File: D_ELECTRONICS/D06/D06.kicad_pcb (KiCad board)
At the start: 2 copper layers, 17.8 x 17.8 mm, 11 parts, among them J4 Conn_01x02_Female, J5 Conn_01x02_Female, Q1 BSS138

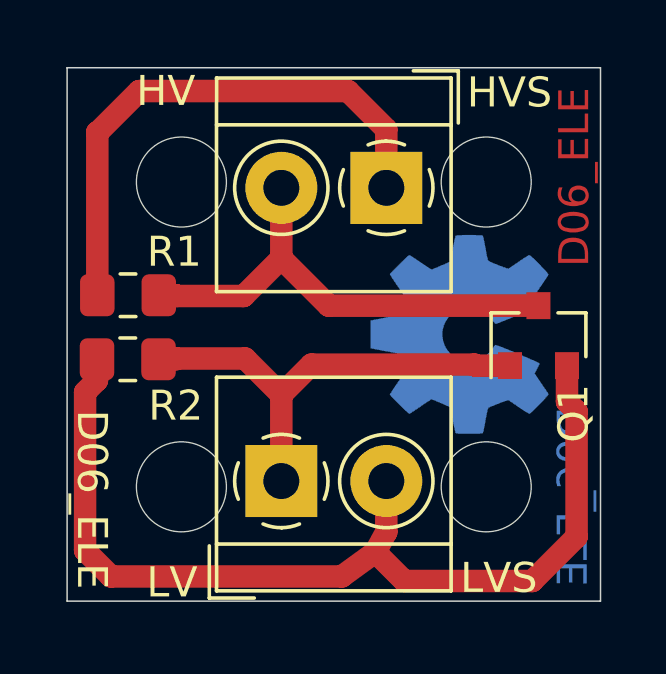
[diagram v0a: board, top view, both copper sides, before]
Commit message: fixed signal trace
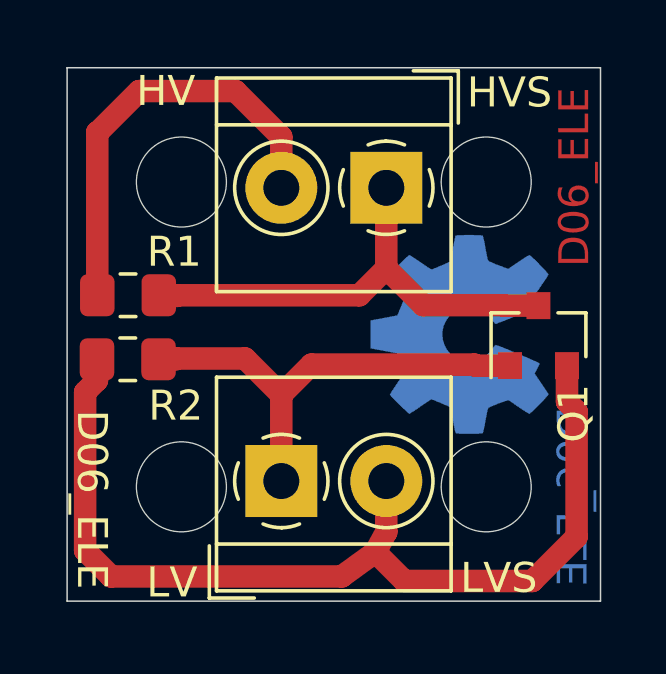
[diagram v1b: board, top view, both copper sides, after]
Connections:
- Q1 pad 3: Net-(J5-Pad2) -> Net-(J5-Pad1)
- R1 pad 1: Net-(J5-Pad1) -> Net-(J5-Pad2)
- R1 pad 2: Net-(J5-Pad2) -> Net-(J5-Pad1)
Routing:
- net Net-(J5-Pad2): track 16.2 -> 14.5 mm
- net Net-(J5-Pad1): track 18.1 -> 16.8 mm
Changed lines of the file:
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@@
     (thickness 1.6)
     (drawings 12)
-    (tracks 36)
+    (tracks 38)
     (zones 0)
     (modules 11)
@@
     (fp_line (start -1 0.6) (end -1 -0.6) (layer F.Fab) (width 0.1))
     (pad 2 smd roundrect (at 1.025 0) (size 1.15 1.4) (layers F.Cu F.Paste F.Mask) (roundrect_rratio 0.217391)
+      (net 4 "Net-(J5-Pad1)"))
+    (pad 1 smd roundrect (at -1.025 0) (size 1.15 1.4) (layers F.Cu F.Paste F.Mask) (roundrect_rratio 0.217391)
       (net 3 "Net-(J5-Pad2)"))
-    (pad 1 smd roundrect (at -1.025 0) (size 1.15 1.4) (layers F.Cu F.Paste F.Mask) (roundrect_rratio 0.217391)
-      (net 4 "Net-(J5-Pad1)"))
     (model ${KISYS3DMOD}/Resistor_SMD.3dshapes/R_0805_2012Metric.wrl
       (at (xyz 0 0 0))
@@
     )
     (pad 3 smd rect (at 1 0 90) (size 0.9 0.8) (layers F.Cu F.Paste F.Mask)
-      (net 3 "Net-(J5-Pad2)"))
+      (net 4 "Net-(J5-Pad1)"))
     (pad 2 smd rect (at -1 0.95 90) (size 0.9 0.8) (layers F.Cu F.Paste F.Mask)
       (net 1 "Net-(J4-Pad2)"))
@@
   (segment (start 25.9336 29.6926) (end 27.14 30.899) (width 0.75) (layer F.Cu) (net 2))
   (segment (start 23.6472 29.6926) (end 25.9336 29.6926) (width 0.75) (layer F.Cu) (net 2))
-  (segment (start 35.7124 27.9306) (end 28.718 27.9306) (width 0.75) (layer F.Cu) (net 3))
-  (segment (start 27.14 26.3526) (end 27.14 24.003) (width 0.75) (layer F.Cu) (net 3))
-  (segment (start 28.718 27.9306) (end 27.14 26.3526) (width 0.75) (layer F.Cu) (net 3))
-  (segment (start 23.6308 27.5844) (end 23.6562 27.6098) (width 0.75) (layer F.Cu) (net 3))
-  (segment (start 23.0558 27.5844) (end 23.6308 27.5844) (width 0.75) (layer F.Cu) (net 3))
-  (segment (start 25.8828 27.6098) (end 27.14 26.3526) (width 0.75) (layer F.Cu) (net 3))
-  (segment (start 23.6562 27.6098) (end 25.8828 27.6098) (width 0.75) (layer F.Cu) (net 3))
-  (segment (start 21.0058 22.1488) (end 21.0058 27.5844) (width 0.75) (layer F.Cu) (net 4))
-  (segment (start 21.0185 22.1615) (end 21.0058 22.1488) (width 0.75) (layer F.Cu) (net 4))
-  (segment (start 22.4028 20.7772) (end 21.0185 22.1615) (width 0.75) (layer F.Cu) (net 4))
-  (segment (start 29.3642 20.7772) (end 22.4028 20.7772) (width 0.75) (layer F.Cu) (net 4))
-  (segment (start 30.64 24.003) (end 30.64 22.053) (width 0.75) (layer F.Cu) (net 4))
-  (segment (start 30.64 22.053) (end 29.3642 20.7772) (width 0.75) (layer F.Cu) (net 4))
+  (segment (start 22.4028 20.7772) (end 21.0185 22.1615) (width 0.75) (layer F.Cu) (net 3))
+  (segment (start 21.0058 22.1488) (end 21.0058 27.5844) (width 0.75) (layer F.Cu) (net 3))
+  (segment (start 25.611256 20.7772) (end 22.4028 20.7772) (width 0.75) (layer F.Cu) (net 3))
+  (segment (start 21.0185 22.1615) (end 21.0058 22.1488) (width 0.75) (layer F.Cu) (net 3))
+  (segment (start 27.14 22.305944) (end 25.611256 20.7772) (width 0.75) (layer F.Cu) (net 3))
+  (segment (start 27.14 24.003) (end 27.14 22.305944) (width 0.75) (layer F.Cu) (net 3))
+  (segment (start 23.6308 27.5844) (end 23.6562 27.6098) (width 0.75) (layer F.Cu) (net 4))
+  (segment (start 23.0558 27.5844) (end 23.6308 27.5844) (width 0.75) (layer F.Cu) (net 4))
+  (segment (start 30.64 26.6878) (end 30.64 24.003) (width 0.75) (layer F.Cu) (net 4))
+  (segment (start 23.0558 27.5844) (end 29.7434 27.5844) (width 0.75) (layer F.Cu) (net 4))
+  (segment (start 29.7434 27.5844) (end 30.64 26.6878) (width 0.75) (layer F.Cu) (net 4))
+  (segment (start 34.5624 27.9306) (end 34.5464 27.9146) (width 0.75) (layer F.Cu) (net 4))
+  (segment (start 35.7124 27.9306) (end 34.5624 27.9306) (width 0.75) (layer F.Cu) (net 4))
+  (segment (start 31.8668 27.9146) (end 30.64 26.6878) (width 0.75) (layer F.Cu) (net 4))
+  (segment (start 34.5464 27.9146) (end 31.8668 27.9146) (width 0.75) (layer F.Cu) (net 4))
 )
